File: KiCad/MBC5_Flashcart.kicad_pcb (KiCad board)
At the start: 2 copper layers, 51.1 x 61.3 mm, 10 parts, among them J0 CartBus, U1 MBC5, U2 MBM29F033C, U3 FM18W08

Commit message: Update to V2
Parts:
- removed ? (x2): , 
- added C5: 100nF, Capacitor_SMD:C_0603_1608Metric, F.Cu at (120.1, 111.3)
- added H1: 3x3 Ground Pad, Custom:Nintendo_3x3_GNDPad, F.Cu at (120.1, 72.3)
- added JP1: Jumper_NO_Small, Jumper:SolderJumper-2_P1.3mm_Open_RoundedPad1.0x1.5mm, F.Cu at (161.1, 71.4)
- added PAD*: GBA-ProductionIndicator, Custom:GBA-ProductionIndicator, B.Cu at (156.7, 77.9)
- added R1: 10K, Resistor_SMD:R_0603_1608Metric, F.Cu at (137.2, 106.1)
- added ROM Mode: SW_SP3T, Custom:CUS-13TB-Aliex SP3T, F.Cu at (161.1, 79.5)
- added U4: 74LVC1G332GW,125, Package_SO:TSOP-6_1.65x3.05mm_P0.95mm, F.Cu at (120.0, 107.7)
- moved C4 30.4 mm to (164.5, 95.1), turned to -90 degrees
- moved U2 18.5 mm to (158.1, 103.9), turned to -90 degrees
- moved U3 18.3 mm to (128.7, 105.5)
- moved C3 18.1 mm to (164.5, 113.4), turned to -90 degrees
- moved U1 16.1 mm to (127.9, 84.8)
- moved C1 14.8 mm to (125.6, 77.1)
- moved C2 13.9 mm to (135.0, 93.3), turned to 90 degrees
- moved J0 11.9 mm to (142.6, 130.0)
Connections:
- U1 pad 22: RA21 -> RA21_MBC
- U1 pad 25: Net-(U1-Pad25) -> unconnected-(U1-Pad25)
- U1 pad 26: Net-(U1-Pad26) -> unconnected-(U1-Pad26)
- U1 pad 27: Net-(U1-Pad27) -> unconnected-(U1-Pad27)
- U2 pad 11: Net-(U2-Pad11) -> unconnected-(U2-Pad11)
- U2 pad 36: Net-(U2-Pad36) -> unconnected-(U2-Pad36)
- U3 pad 20: RAMCS -> #CE
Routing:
- net +5V: track 105.8 -> 175.9 mm, vias 3 -> 7
- net RA21_MBC: track 0.00 -> 56.0 mm, vias 0 -> 2
- net GND: track 141.0 -> 99.0 mm, vias 3 -> 14
- net A7: track 48.4 -> 89.3 mm
- net A6: track 49.3 -> 88.4 mm
- net A10: track 37.6 -> 76.7 mm, vias 2 -> 0
- net D1: track 107.8 -> 70.2 mm, vias 1 -> 2
- net D2: track 106.7 -> 69.1 mm, vias 1 -> 2
- net D0: track 106.3 -> 70.9 mm
- net A5: track 52.6 -> 87.4 mm
- net D7: track 105.7 -> 71.5 mm
- net D3: track 97.1 -> 62.9 mm
- net D6: track 103.2 -> 69.7 mm
- net D4: track 98.3 -> 65.5 mm
- net D5: track 100.7 -> 68.6 mm
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- removed copper zone on F.Cu, net +5V
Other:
- board size 51.1 x 61.3 mm -> 51 x 60.7 mm
- net class Default removed
- rule pad_to_mask_clearance: 0.05 -> 0
- board text added: "'22"
- board text added: "1"
- board text added: "12"
- board text added: "4MB"
- board text added: "6"
- board text added: "7"
- board text added: "Bank A"
- board text added: "Bank B"
- board text removed: "BOM: U1: MBC5 U2: MBM29F033C/AM29F032 U3: FM18W08 C1,C2,C3,C4: 100nF 0603 Capacitor"
- board text removed: "C1"
- board text removed: "C2"
- board text removed: "C4"
- board text removed: "JLCJLCJLCJLC"
- board text removed: "U1"
- board text removed: "U2"
- board text removed: "U3"

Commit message: Release V3
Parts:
- removed PAD*: GBA-ProductionIndicator, Custom:GBA-ProductionIndicator
- added A**: June, HDR_Gameboy_Date_Indicators:08 August, B.Cu at (156.1, 75.7)
- added D1: D, Diode_SMD:D_SOD-123, F.Cu at (145.0, 77.2)
- added M1: Motor_DC, Custom:ANDA-T1035, F.Cu at (144.0, 82.0)
- added Q1: BC817-40,215, Package_TO_SOT_SMD:SOT-23, F.Cu at (150.4, 82.2)
- added R2: 30K, Resistor_SMD:R_0603_1608Metric, F.Cu at (149.4, 78.5)
- added R3: 15Ω, Resistor_SMD:R_0603_1608Metric, F.Cu at (145.0, 75.2)
- added R4: 22Ω, Resistor_SMD:R_0603_1608Metric, F.Cu at (150.2, 85.1)
- J0: footprint Connector_GameBoy:GameBoy_GamePak_CGB-002_P1.50mm_Edge -> HDR_Gameboy_Cartridges:GB_Cartridge
- SW1: renamed from ROM Mode
- moved J0 3.94 mm to (142.6, 126.1)
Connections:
- SW1 pad 0: GND -> (no net)
- U1 pad 26: unconnected-(U1-Pad26) -> Rumble
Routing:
- net GND: track 99.0 -> 139.1 mm, vias 14 -> 6
- net Rumble: track 0.00 -> 30.2 mm, vias 0 -> 2
- net Net-(D1-Pad1): track 0.00 -> 22.1 mm
- net A6: track 88.4 -> 67.9 mm, vias 0 -> 2
- net A7: track 89.3 -> 69.4 mm, vias 0 -> 2
- net A10: track 76.7 -> 57.7 mm, vias 0 -> 2
- net A5: track 87.4 -> 68.6 mm
- net D2: track 69.1 -> 83.6 mm, vias 2 -> 3
- net D0: track 70.9 -> 85.2 mm, vias 1 -> 2
- net RD: track 56.0 -> 68.5 mm, vias 2 -> 3
- net A9: track 70.5 -> 58.6 mm, vias 0 -> 2
- net Net-(D1-Pad2): track 0.00 -> 11.8 mm
- net A11: track 73.5 -> 61.8 mm, vias 0 -> 2
- net #CE: track 18.6 -> 30.3 mm
- net A12: track 73.5 -> 84.5 mm
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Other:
- outline, holes or cut-outs redrawn
- board text removed: "'22"
- board text removed: "1"
- board text removed: "12"
- board text removed: "6"
- board text removed: "7"

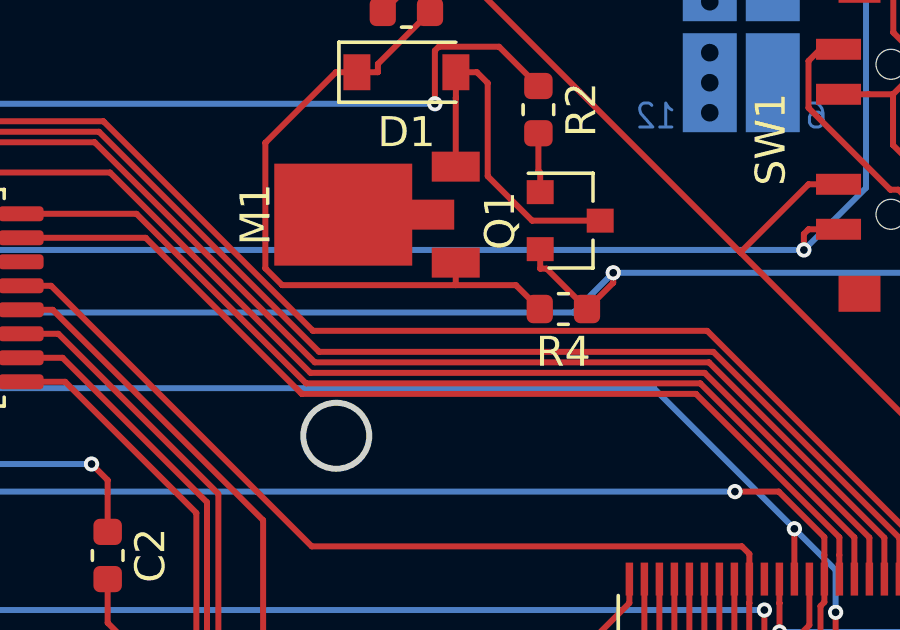
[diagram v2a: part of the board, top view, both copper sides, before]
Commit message: Remove R4
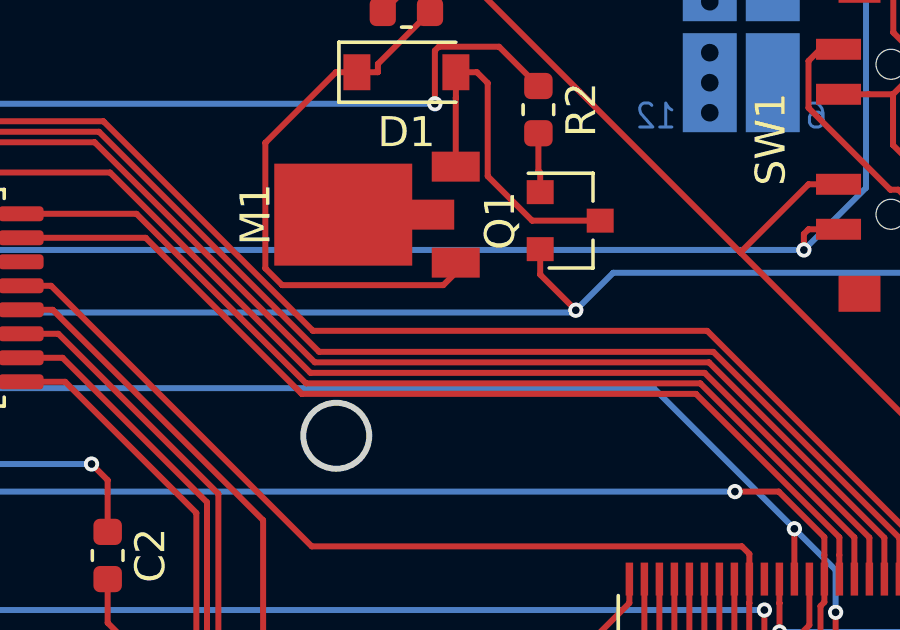
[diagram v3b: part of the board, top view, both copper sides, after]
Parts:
- removed R4: 22Ω, Resistor_SMD:R_0603_1608Metric
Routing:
- net Net-(D1-Pad1): track 22.1 -> 18.7 mm
- net GND: track 139.1 -> 137.3 mm
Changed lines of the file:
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@@
     (fp_arc (start 25 -54.45) (mid 25.353553 -54.303553) (end 25.5 -53.95) (layer "Edge.Cuts") (width 0.2))
     (fp_arc (start 24.7 -4.6) (mid 24.773223 -4.776777) (end 24.95 -4.85) (layer "Edge.Cuts") (width 0.2))
-    (fp_arc (start 24.700002 2.449998) (mid 24.260974 3.510789) (end 23.200441 3.950435) (layer "Edge.Cuts") (width 0.2))
+    (fp_arc (start 24.700002 2.449998) (mid 24.260973 3.510786) (end 23.200441 3.950435) (layer "Edge.Cuts") (width 0.2))
     (fp_arc (start -25.501 -55.75) (mid -25.208107 -56.457107) (end -24.501 -56.75) (layer "Edge.Cuts") (width 0.2))
     (fp_arc (start -25 -4.85) (mid -25.353553 -4.996447) (end -25.5 -5.35) (layer "Edge.Cuts") (width 0.2))
@@
     )
   )
-  (footprint "Resistor_SMD:R_0603_1608Metric" (layer "F.Cu")
-    (at 150.1902 85.1342 180)
-    (descr "Resistor SMD 0603 (1608 Metric), square (rectangular) end terminal, IPC_7351 nominal, (Body size source: http://www.tortai-tech.com/upload/download/2011102023233369053.pdf), generated with kicad-footprint-generator")
-    (tags "resistor")
-    (property "Sheetfile" "MBC5_Flashcart.kicad_sch")
-    (property "Sheetname" "")
-    (attr smd)
-    (fp_text reference "R4" (at 0 -1.43) (layer "F.SilkS")
-      (effects (font (size 1 1) (thickness 0.15)))
-    )
-    (fp_text value "22Ω" (at 0 1.43) (layer "F.Fab")
-      (effects (font (size 1 1) (thickness 0.15)))
-    )
-    (fp_text user "${REFERENCE}" (at 0 0) (layer "F.Fab")
-      (effects (font (size 0.4 0.4) (thickness 0.06)))
-    )
-    (fp_line (start -0.162779 -0.51) (end 0.162779 -0.51) (layer "F.SilkS") (width 0.12))
-    (fp_line (start -0.162779 0.51) (end 0.162779 0.51) (layer "F.SilkS") (width 0.12))
-    (fp_line (start -1.48 0.73) (end -1.48 -0.73) (layer "F.CrtYd") (width 0.05))
-    (fp_line (start 1.48 0.73) (end -1.48 0.73) (layer "F.CrtYd") (width 0.05))
-    (fp_line (start -1.48 -0.73) (end 1.48 -0.73) (layer "F.CrtYd") (width 0.05))
-    (fp_line (start 1.48 -0.73) (end 1.48 0.73) (layer "F.CrtYd") (width 0.05))
-    (fp_line (start 0.8 -0.4) (end 0.8 0.4) (layer "F.Fab") (width 0.1))
-    (fp_line (start -0.8 0.4) (end -0.8 -0.4) (layer "F.Fab") (width 0.1))
-    (fp_line (start 0.8 0.4) (end -0.8 0.4) (layer "F.Fab") (width 0.1))
-    (fp_line (start -0.8 -0.4) (end 0.8 -0.4) (layer "F.Fab") (width 0.1))
-    (pad "1" smd roundrect locked (at -0.7875 0 180) (size 0.875 0.95) (layers "F.Cu" "F.Paste" "F.Mask") (roundrect_rratio 0.25)
-      (net 1 "GND") (pintype "passive"))
-    (pad "2" smd roundrect locked (at 0.7875 0 180) (size 0.875 0.95) (layers "F.Cu" "F.Paste" "F.Mask") (roundrect_rratio 0.25)
-      (net 37 "Net-(D1-Pad1)") (pintype "passive"))
-    (model "${KISYS3DMOD}/Resistor_SMD.3dshapes/R_0603_1608Metric.wrl"
-      (offset (xyz 0 0 0))
-      (scale (xyz 1 1 1))
-      (rotate (xyz 0 0 0))
-    )
-  )
   (footprint "Custom:ANDA-T1035" (layer "F.Cu")
     (at 143.9778 81.9886 180)
@@
   (segment (start 156.8904 113.636) (end 156.8904 111.4606) (width 0.2) (layer "F.Cu") (net 1))
   (segment (start 121.119 71.5517) (end 120.3687 71.5517) (width 0.2) (layer "F.Cu") (net 1))
-  (segment (start 150.9777 85.1342) (end 151.8522 84.2597) (width 0.2) (layer "F.Cu") (net 1))
   (segment (start 165.62 120.402) (end 165.62 115.3107) (width 0.2) (layer "F.Cu") (net 1))
   (segment (start 166.12 120.69) (end 166.12 123.6102) (width 1.5) (layer "F.Cu") (net 1))
@@
   (segment (start 156.3904 113.636) (end 156.3904 111.4526) (width 0.2) (layer "F.Cu") (net 1))
   (segment (start 121.7475 113.755) (end 124.05 113.755) (width 0.2) (layer "F.Cu") (net 1))
+  (segment (start 149.4178 83.1386) (end 149.4178 83.9874) (width 0.2) (layer "F.Cu") (net 1))
   (segment (start 165.2086 111.455) (end 165.2086 113.4469) (width 0.2) (layer "F.Cu") (net 1))
   (segment (start 120.3687 71.5517) (end 120.119 71.302) (width 0.2) (layer "F.Cu") (net 1))
@@
   (segment (start 127.54 88.935) (end 127.54 90.3666) (width 0.2) (layer "F.Cu") (net 1))
   (segment (start 126.4175 77.08) (end 125.94 77.5575) (width 0.2) (layer "F.Cu") (net 1))
-  (segment (start 151.8522 84.2597) (end 151.8522 83.9268) (width 0.2) (layer "F.Cu") (net 1))
   (segment (start 166.12 126.21) (end 166.12 126.2102) (width 0.2) (layer "F.Cu") (net 1))
   (segment (start 121.119 71.9268) (end 121.119 71.5517) (width 0.2) (layer "F.Cu") (net 1))
   (segment (start 164.4824 95.8851) (end 164.4824 110.7288) (width 0.2) (layer "F.Cu") (net 1))
   (segment (start 165.2086 113.4469) (end 164.4824 114.1731) (width 0.2) (layer "F.Cu") (net 1))
-  (segment (start 149.4178 83.1386) (end 149.4178 83.7889) (width 0.2) (layer "F.Cu") (net 1))
-  (segment (start 149.4178 83.7889) (end 149.6324 83.7889) (width 0.2) (layer "F.Cu") (net 1))
   (segment (start 165.62 115.3107) (end 164.4824 114.1731) (width 0.2) (layer "F.Cu") (net 1))
   (segment (start 135 92.5625) (end 135 90.8378) (width 0.2) (layer "F.Cu") (net 1))
   (segment (start 125.94 83.3171) (end 125.94 80.585) (width 0.2) (layer "F.Cu") (net 1))
   (segment (start 164.4824 110.7288) (end 165.2086 111.455) (width 0.2) (layer "F.Cu") (net 1))
+  (segment (start 149.4178 83.9874) (end 150.6047 85.1743) (width 0.2) (layer "F.Cu") (net 1))
   (segment (start 165.62 120.402) (end 165.832 120.402) (width 0.2) (layer "F.Cu") (net 1))
   (segment (start 121.119 72.302) (end 121.119 71.9268) (width 0.2) (layer "F.Cu") (net 1))
   (segment (start 163.6252 83.4266) (end 165.2094 85.0108) (width 0.2) (layer "F.Cu") (net 1))
-  (segment (start 149.6324 83.7889) (end 150.9777 85.1342) (width 0.2) (layer "F.Cu") (net 1))
   (segment (start 165.2094 95.1581) (end 164.4824 95.8851) (width 0.2) (layer "F.Cu") (net 1))
   (segment (start 165.2094 85.0108) (end 165.2094 95.1581) (width 0.2) (layer "F.Cu") (net 1))
@@
   (via (at 163.6252 83.4266) (size 0.508) (drill 0.254) (layers "F.Cu" "B.Cu") (net 1))
   (via (at 165.62 120.402) (size 2.37) (drill 2) (layers "F.Cu" "B.Cu") (net 1))
-  (via (at 151.8522 83.9268) (size 0.508) (drill 0.254) (layers "F.Cu" "B.Cu") (net 1))
+  (via (at 150.6047 85.1743) (size 0.508) (drill 0.254) (layers "F.Cu" "B.Cu") (net 1))
   (via (at 127.8744 85.2515) (size 0.508) (drill 0.254) (layers "F.Cu" "B.Cu") (net 1))
   (via (at 127.5334 90.3732) (size 0.508) (drill 0.254) (layers "F.Cu" "B.Cu") (net 1))
   (via (at 134.4634 90.3012) (size 0.508) (drill 0.254) (layers "F.Cu" "B.Cu") (net 1))
-  (segment (start 151.8522 83.9268) (end 150.5275 85.2515) (width 0.2) (layer "B.Cu") (net 1))
   (segment (start 163.125 83.9268) (end 151.8522 83.9268) (width 0.2) (layer "B.Cu") (net 1))
   (segment (start 150.5275 85.2515) (end 127.8744 85.2515) (width 0.2) (layer "B.Cu") (net 1))
@@
   (segment (start 126.2286 86.8973) (end 127.8744 85.2515) (width 0.2) (layer "B.Cu") (net 1))
   (segment (start 126.2286 87.9763) (end 126.2286 86.8973) (width 0.2) (layer "B.Cu") (net 1))
+  (segment (start 150.6047 85.1743) (end 150.5275 85.2515) (width 0.2) (layer "B.Cu") (net 1))
+  (segment (start 151.8522 83.9268) (end 150.6047 85.1743) (width 0.2) (layer "B.Cu") (net 1))
   (segment (start 134.4634 90.3012) (end 128.5535 90.3012) (width 0.2) (layer "B.Cu") (net 1))
   (segment (start 135.6006 96.1956) (end 134.7808 97.0154) (width 0.2) (layer "F.Cu") (net 2))
@@
   (segment (start 121.05 105.4386) (end 121.4747 105.0139) (width 0.2) (layer "B.Cu") (net 35))
   (segment (start 129.0279 105.0139) (end 131.733 102.3088) (width 0.2) (layer "B.Cu") (net 35))
-  (segment (start 146.6028 84.3389) (end 140.8164 84.3389) (width 0.2) (layer "F.Cu") (net 37))
+  (segment (start 146.6028 83.5886) (end 146.6028 83.924) (width 0.2) (layer "F.Cu") (net 37))
   (segment (start 144.0081 76.9654) (end 145.7453 75.2282) (width 0.2) (layer "F.Cu") (net 37))
   (segment (start 140.2558 79.5931) (end 142.6075 77.2414) (width 0.2) (layer "F.Cu") (net 37))
   (segment (start 143.3078 77.2414) (end 144.0081 77.2414) (width 0.2) (layer "F.Cu") (net 37))
   (segment (start 143.3078 77.2414) (end 142.6075 77.2414) (width 0.2) (layer "F.Cu") (net 37))
-  (segment (start 146.6028 83.5886) (end 146.6028 84.3389) (width 0.2) (layer "F.Cu") (net 37))
   (segment (start 140.8164 84.3389) (end 140.2558 83.7783) (width 0.2) (layer "F.Cu") (net 37))
+  (segment (start 146.1879 84.3389) (end 140.8164 84.3389) (width 0.2) (layer "F.Cu") (net 37))
   (segment (start 140.2558 83.7783) (end 140.2558 79.5931) (width 0.2) (layer "F.Cu") (net 37))
-  (segment (start 149.4027 85.1342) (end 148.6074 84.3389) (width 0.2) (layer "F.Cu") (net 37))
+  (segment (start 146.6028 83.924) (end 146.1879 84.3389) (width 0.2) (layer "F.Cu") (net 37))
   (segment (start 144.0081 77.2414) (end 144.0081 76.9654) (width 0.2) (layer "F.Cu") (net 37))
-  (segment (start 148.6074 84.3389) (end 146.6028 84.3389) (width 0.2) (layer "F.Cu") (net 37))
   (segment (start 161.1789 79.6703) (end 161.1789 77.9766) (width 0.2) (layer "F.Cu") (net 38))
   (segment (start 161.3904 113.636) (end 161.3904 113.1074) (width 0.2) (layer "F.Cu") (net 38))
